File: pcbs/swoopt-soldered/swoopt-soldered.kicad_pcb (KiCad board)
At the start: 2 copper layers, 137.6 x 110.1 mm, 80 parts, among them J1 TRRS, SW1 MX, SW10 MX, SW11 MX, SW12 MX, SW13 MX, SW14 MX, SW15 MX, SW16 MX, SW17 MX, SW18 MX, SW19 MX, SW2 MX, SW20 MX, SW21 MX, SW3 MX, SW4 MX, SW5 MX, SW6 MX, SW7 MX, SW8 MX, SW9 MX

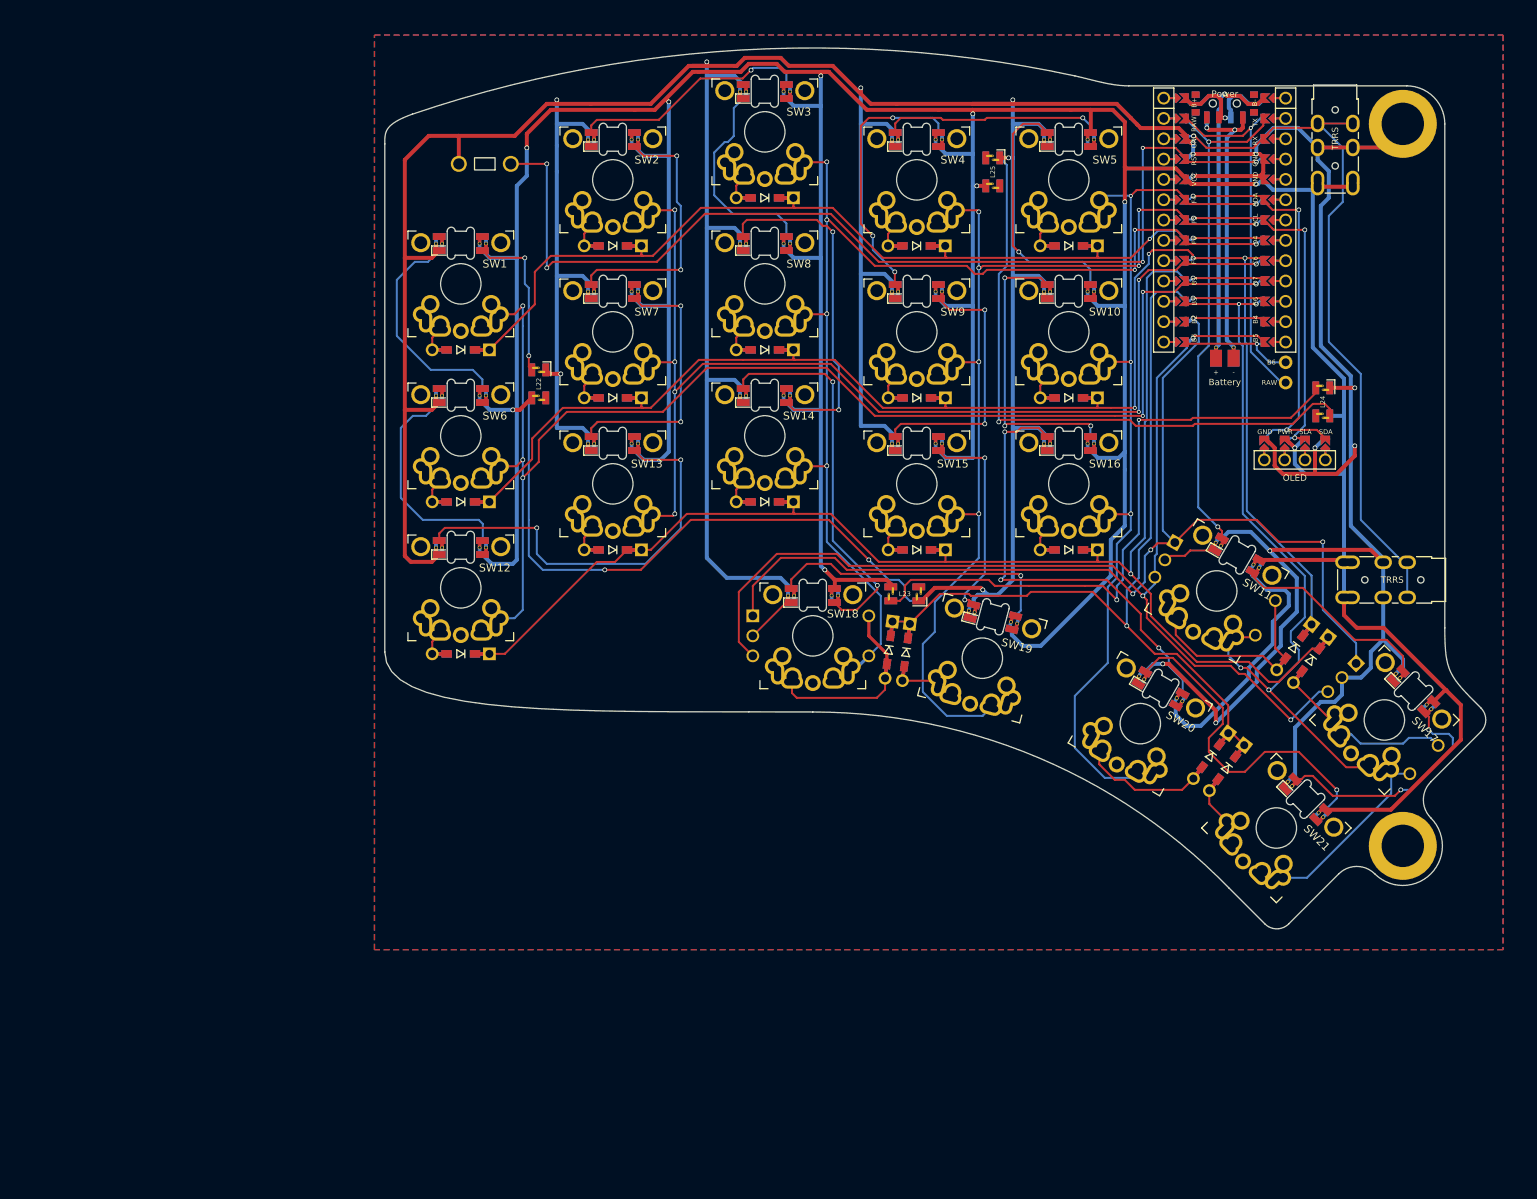
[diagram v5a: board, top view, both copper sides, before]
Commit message: added m2 screw holes for mounting
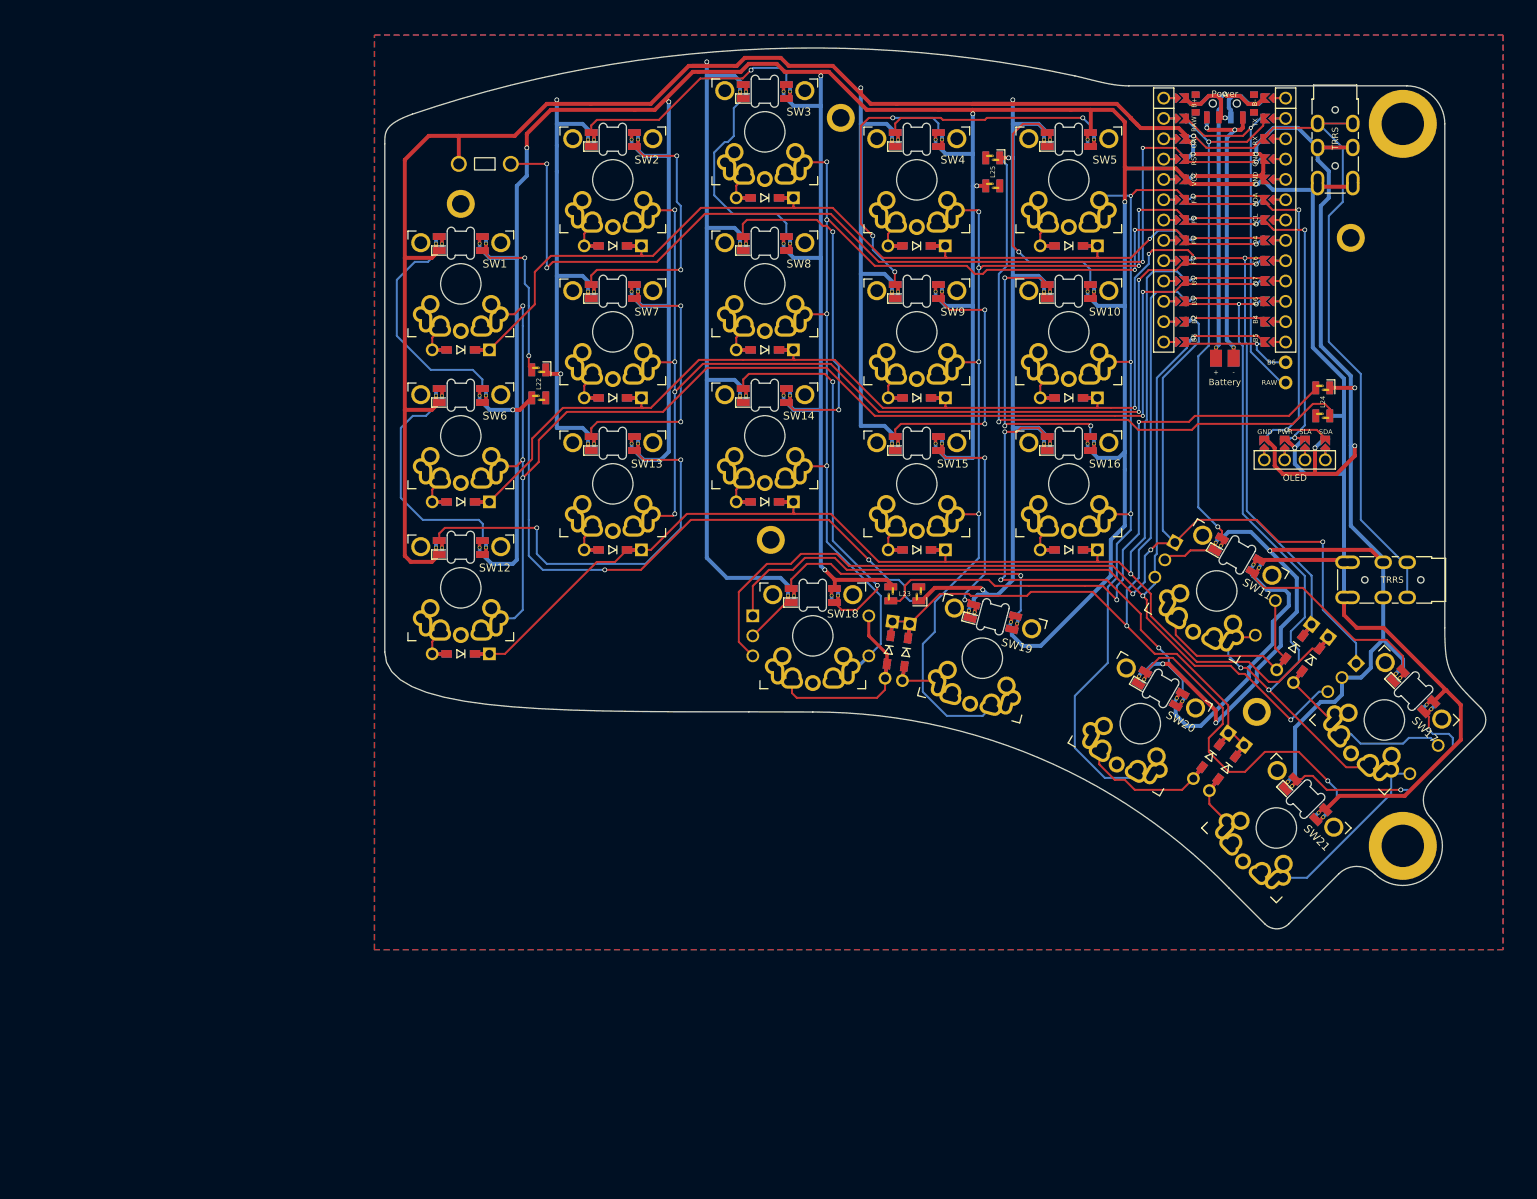
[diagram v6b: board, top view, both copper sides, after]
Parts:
- added REF**: MountingHole_2.2mm_M2_ISO7380_Pad, MountingHole:MountingHole_2.2mm_M2_ISO7380_Pad, F.Cu at (205.2, 67.2)
- added REF**: MountingHole_2.2mm_M2_ISO7380_Pad, MountingHole:MountingHole_2.2mm_M2_ISO7380_Pad, F.Cu at (193.5, 126.5)
- added REF**: MountingHole_2.2mm_M2_ISO7380_Pad, MountingHole:MountingHole_2.2mm_M2_ISO7380_Pad, F.Cu at (132.8, 105.0)
- added REF**: MountingHole_2.2mm_M2_ISO7380_Pad, MountingHole:MountingHole_2.2mm_M2_ISO7380_Pad, F.Cu at (141.5, 52.2)
- added REF**: MountingHole_2.2mm_M2_ISO7380_Pad, MountingHole:MountingHole_2.2mm_M2_ISO7380_Pad, F.Cu at (94.0, 63.0)
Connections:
- REF** pad 1: GND -> (no net) (x2)
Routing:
- net GND: track 723.9 -> 716.4 mm
- net Net-(L17-DOUT): track 30.6 -> 30.0 mm
